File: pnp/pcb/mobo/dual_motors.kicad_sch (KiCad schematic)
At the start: 9 parts, among them M5 MOTOR1, M6 MOTOR2

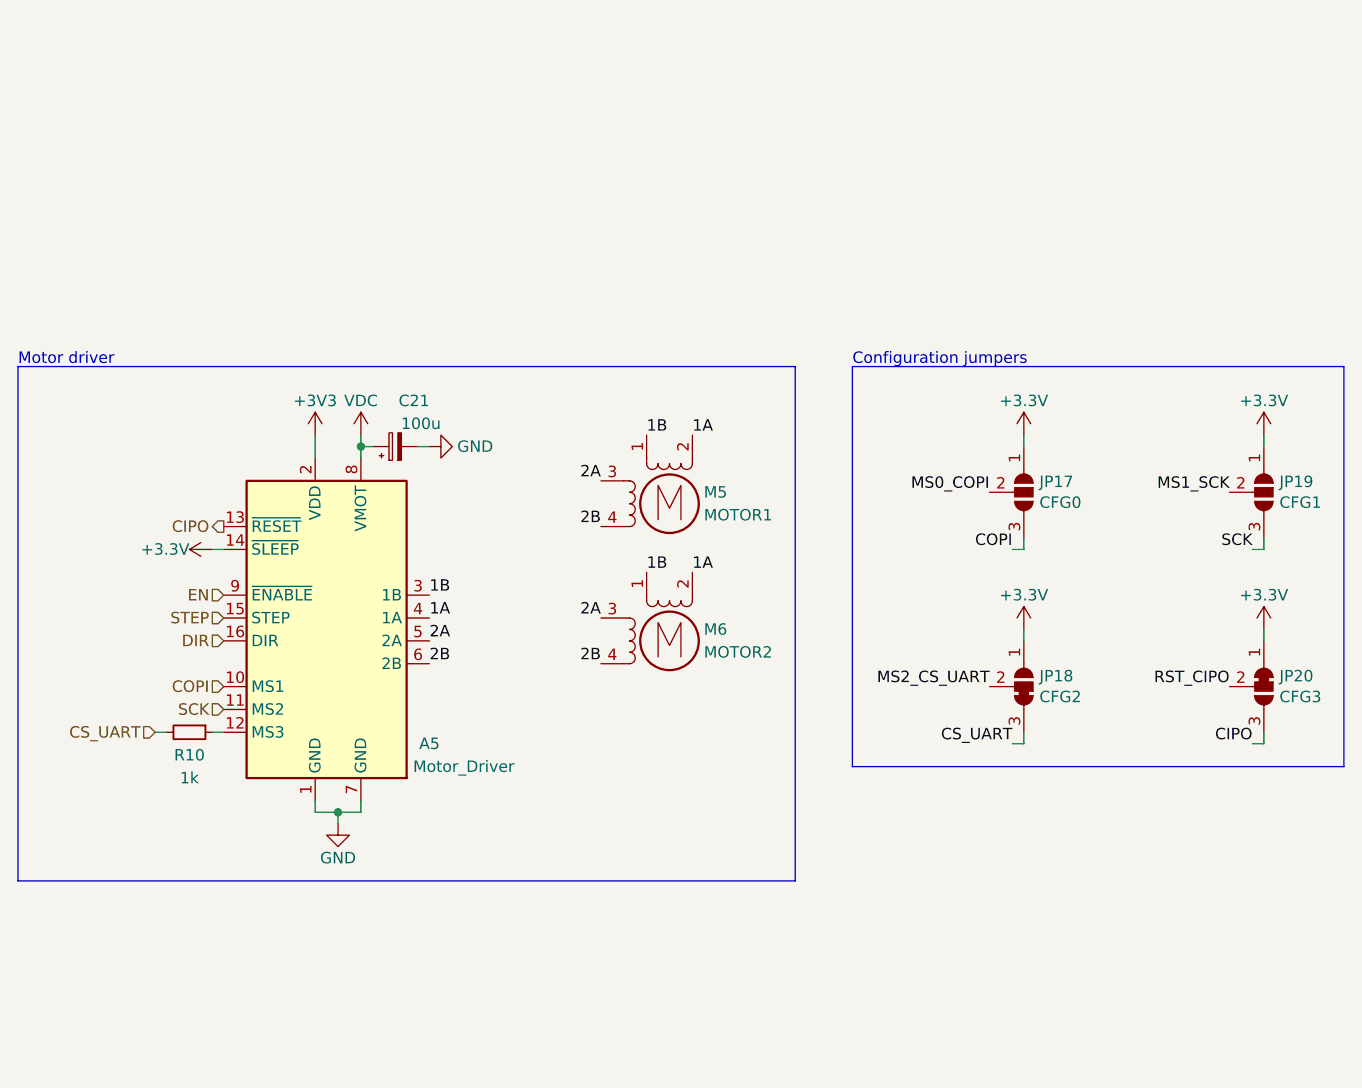
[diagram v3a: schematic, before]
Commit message: Connect all sub-sheets together
Refactored schematic is checked against existing lay-out.
Connectivity has stayed the same.
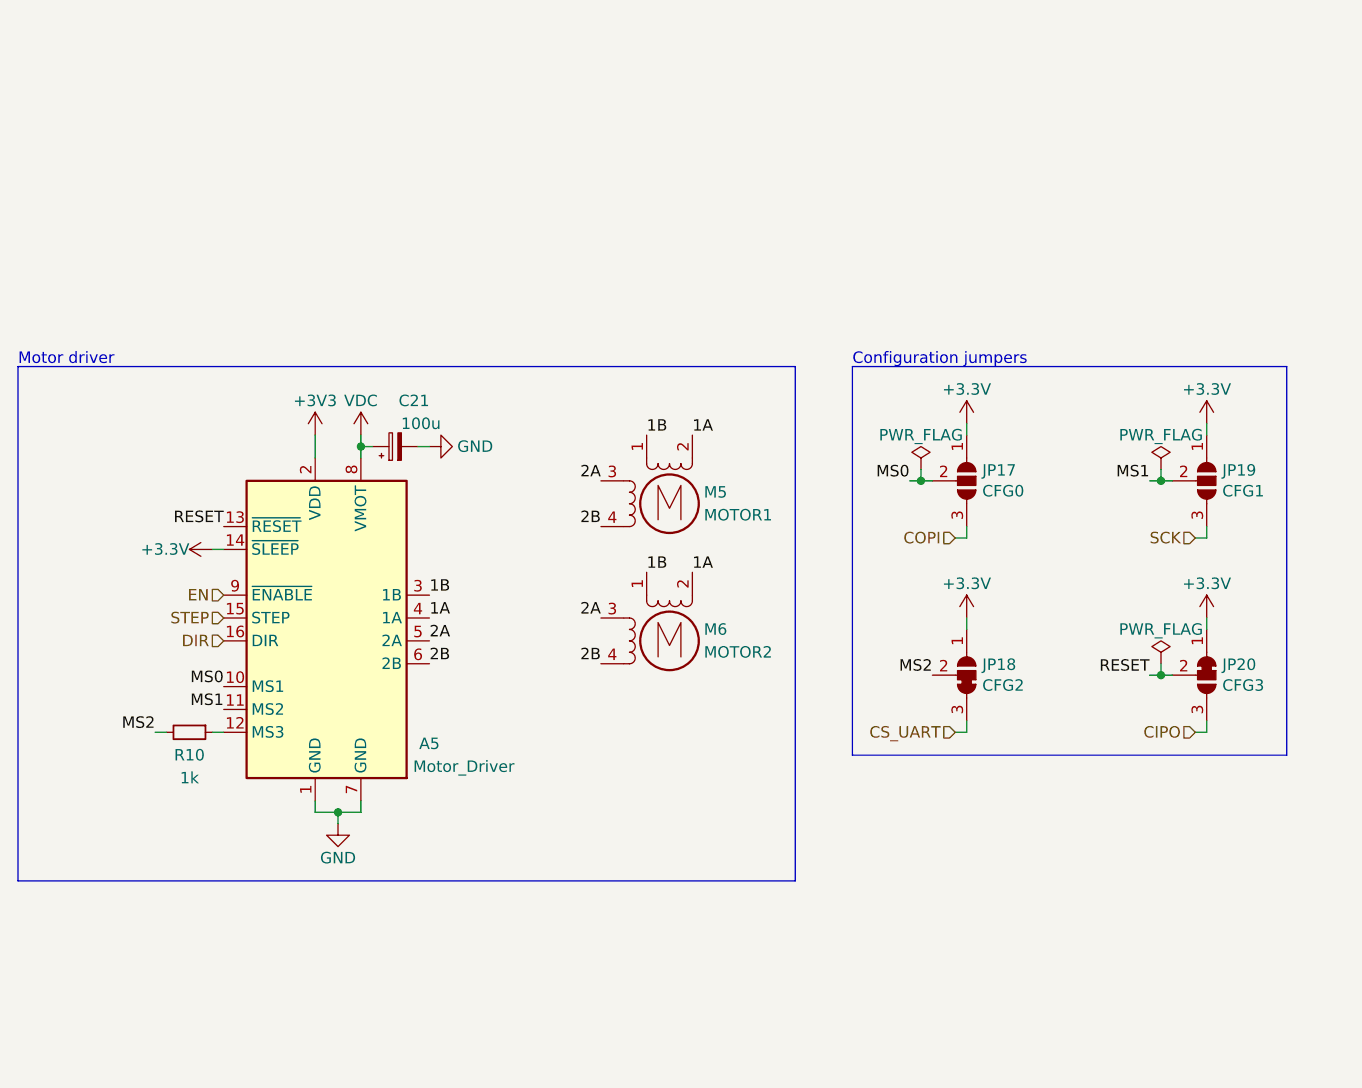
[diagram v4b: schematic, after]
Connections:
- net CIPO: no longer A5.13 (~{RESET})
- net COPI: no longer A5.10 (MS1)
- net CS_UART: no longer R10.2
- net SCK: no longer A5.11 (MS2)
- net MS0_COPI renamed MS0
- net MS0: now also A5.10 (MS1)
- net MS1_SCK renamed MS1
- net MS1: now also A5.11 (MS2)
- net MS2_CS_UART renamed MS2
- net MS2: now also R10.2
- net RST_CIPO renamed RESET
- net RESET: now also A5.13 (~{RESET})
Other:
- moved on the sheet: JP17, JP18, JP19, JP20

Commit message: Fixed schematic parity
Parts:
- JP18: footprint index:SolderJumper-3_P1.3mm_Bridged23_RoundedPad1.0x1.5mm -> (none)
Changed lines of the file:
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@@
     (effects (font (size 1.27 1.27)) (justify right))
   )
-  (symbol (lib_id "power:+3V3") (at 116.84 85.09 0)
+  (symbol (lib_id "power:+3V3") (at 116.84 85.09 0) (unit 1)
     (in_bom yes) (on_board yes)
     (property "Reference" "#PWR066" (id 0) (at 116.84 88.9 0)
@@
     (pin "1")
   )
-  (symbol (lib_id "power:GND") (at 119.38 128.27 0)
+  (symbol (lib_id "power:GND") (at 119.38 128.27 0) (unit 1)
     (in_bom yes) (on_board yes)
     (property "Reference" "#PWR067" (id 0) (at 119.38 134.62 0)
@@
     (pin "1")
   )
-  (symbol (lib_id "power:+3.3V") (at 105.41 97.79 90)
+  (symbol (lib_id "power:+3.3V") (at 105.41 97.79 90) (unit 1)
     (in_bom yes) (on_board yes)
     (property "Reference" "#PWR065" (id 0) (at 109.22 97.79 0)
@@
     (pin "1")
   )
-  (symbol (lib_id "Motor:Stepper_Motor_bipolar") (at 156.21 107.95 0)
+  (symbol (lib_id "Motor:Stepper_Motor_bipolar") (at 156.21 107.95 0) (unit 1)
     (in_bom yes) (on_board yes)
     (property "Reference" "M6" (id 0) (at 160.02 106.68 0)
@@
     (pin "4")
   )
-  (symbol (lib_id "Motor:Stepper_Motor_bipolar") (at 156.21 92.71 0)
+  (symbol (lib_id "Motor:Stepper_Motor_bipolar") (at 156.21 92.71 0) (unit 1)
     (in_bom yes) (on_board yes)
     (property "Reference" "M5" (id 0) (at 160.02 91.44 0)
@@
     (pin "4")
   )
-  (symbol (lib_id "Driver_Motor:Pololu_Breakout_A4988") (at 116.84 105.41 0)
+  (symbol (lib_id "Driver_Motor:Pololu_Breakout_A4988") (at 116.84 105.41 0) (unit 1)
     (in_bom yes) (on_board yes)
     (property "Reference" "A5" (id 0) (at 129.54 119.38 0))
@@
     (pin "9")
   )
-  (symbol (lib_id "power:VDC") (at 121.92 85.09 0)
+  (symbol (lib_id "power:VDC") (at 121.92 85.09 0) (unit 1)
     (in_bom yes) (on_board yes)
     (property "Reference" "#PWR068" (id 0) (at 121.92 87.63 0)
@@
     (pin "1")
   )
-  (symbol (lib_id "Device:C_Polarized_Small") (at 125.73 86.36 90)
+  (symbol (lib_id "Device:C_Polarized_Small") (at 125.73 86.36 90) (unit 1)
     (in_bom yes) (on_board yes)
     (property "Reference" "C21" (id 0) (at 129.54 81.28 90)
@@
     (pin "2")
   )
-  (symbol (lib_id "power:GND") (at 129.54 86.36 90)
+  (symbol (lib_id "power:GND") (at 129.54 86.36 90) (unit 1)
     (in_bom yes) (on_board yes)
     (property "Reference" "#PWR072" (id 0) (at 135.89 86.36 0)
@@
     (pin "1")
   )
-  (symbol (lib_id "power:+3.3V") (at 215.9 105.41 0)
+  (symbol (lib_id "power:+3.3V") (at 215.9 105.41 0) (unit 1)
     (in_bom yes) (on_board yes)
     (property "Reference" "#PWR070" (id 0) (at 215.9 109.22 0)
@@
     (pin "1")
   )
-  (symbol (lib_id "power:+3.3V") (at 189.23 83.82 0)
+  (symbol (lib_id "power:+3.3V") (at 189.23 83.82 0) (unit 1)
     (in_bom yes) (on_board yes)
     (property "Reference" "#PWR063" (id 0) (at 189.23 87.63 0)
@@
     (pin "1")
   )
-  (symbol (lib_id "power:+3.3V") (at 215.9 83.82 0)
+  (symbol (lib_id "power:+3.3V") (at 215.9 83.82 0) (unit 1)
     (in_bom yes) (on_board yes)
     (property "Reference" "#PWR069" (id 0) (at 215.9 87.63 0)
@@
     (pin "1")
   )
-  (symbol (lib_id "power:+3.3V") (at 189.23 105.41 0)
+  (symbol (lib_id "power:+3.3V") (at 189.23 105.41 0) (unit 1)
     (in_bom yes) (on_board yes)
     (property "Reference" "#PWR064" (id 0) (at 189.23 109.22 0)
@@
     (pin "1")
   )
-  (symbol (lib_id "Jumper:SolderJumper_3_Open") (at 189.23 90.17 270)
+  (symbol (lib_id "Jumper:SolderJumper_3_Open") (at 189.23 90.17 270) (unit 1)
     (in_bom yes) (on_board yes)
     (property "Reference" "JP17" (id 0) (at 190.9572 89.0016 90)
@@
     (pin "3")
   )
-  (symbol (lib_id "Jumper:SolderJumper_3_Bridged12") (at 215.9 111.76 270)
+  (symbol (lib_id "Jumper:SolderJumper_3_Bridged12") (at 215.9 111.76 270) (unit 1)
     (in_bom yes) (on_board yes)
     (property "Reference" "JP20" (id 0) (at 217.6272 110.5916 90)
@@
     (pin "3")
   )
-  (symbol (lib_id "Jumper:SolderJumper_3_Open") (at 215.9 90.17 270)
+  (symbol (lib_id "Jumper:SolderJumper_3_Open") (at 215.9 90.17 270) (unit 1)
     (in_bom yes) (on_board yes)
     (property "Reference" "JP19" (id 0) (at 217.6272 89.0016 90)
@@
     (pin "3")
   )
-  (symbol (lib_id "Device:R_Small") (at 102.87 118.11 270)
+  (symbol (lib_id "Device:R_Small") (at 102.87 118.11 270) (unit 1)
     (in_bom yes) (on_board yes)
     (property "Reference" "R10" (id 0) (at 102.87 120.65 90))
@@
     (pin "2")
   )
-  (symbol (lib_id "index:SolderJumper_3_Bridged23") (at 189.23 111.76 270) (mirror x)
+  (symbol (lib_id "index:SolderJumper_3_Bridged23") (at 189.23 111.76 270) (mirror x) (unit 1)
     (in_bom yes) (on_board yes)
     (property "Reference" "JP18" (id 0) (at 190.9572 110.5916 90)
@@
       (effects (font (size 1.27 1.27)) (justify left))
     )
-    (property "Footprint" "index:SolderJumper-3_P1.3mm_Bridged23_RoundedPad1.0x1.5mm" (id 2) (at 189.23 111.76 0)
+    (property "Footprint" "" (id 2) (at 189.23 111.76 0)
       (effects (font (size 1.27 1.27)) hide)
     )
@@
     (pin "3")
   )
-  (symbol (lib_id "power:PWR_FLAG") (at 210.82 88.9 0)
+  (symbol (lib_id "power:PWR_FLAG") (at 210.82 88.9 0) (unit 1)
     (in_bom yes) (on_board yes)
     (property "Reference" "#FLG06" (id 0) (at 210.82 86.995 0)
@@
     (pin "1")
   )
-  (symbol (lib_id "power:PWR_FLAG") (at 210.82 110.49 0)
+  (symbol (lib_id "power:PWR_FLAG") (at 210.82 110.49 0) (unit 1)
     (in_bom yes) (on_board yes)
     (property "Reference" "#FLG07" (id 0) (at 210.82 108.585 0)
@@
     (pin "1")
   )
-  (symbol (lib_id "power:PWR_FLAG") (at 184.15 88.9 0)
+  (symbol (lib_id "power:PWR_FLAG") (at 184.15 88.9 0) (unit 1)
     (in_bom yes) (on_board yes)
     (property "Reference" "#FLG05" (id 0) (at 184.15 86.995 0)

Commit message: Fix symbol library
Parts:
- JP18: footprint (none) -> index:SolderJumper-3_P1.3mm_Bridged23_RoundedPad1.0x1.5mm
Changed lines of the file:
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@@
       (effects (font (size 1.27 1.27)) (justify left))
     )
-    (property "Footprint" "" (id 2) (at 189.23 111.76 0)
+    (property "Footprint" "index:SolderJumper-3_P1.3mm_Bridged23_RoundedPad1.0x1.5mm" (id 2) (at 189.23 111.76 0)
       (effects (font (size 1.27 1.27)) hide)
     )

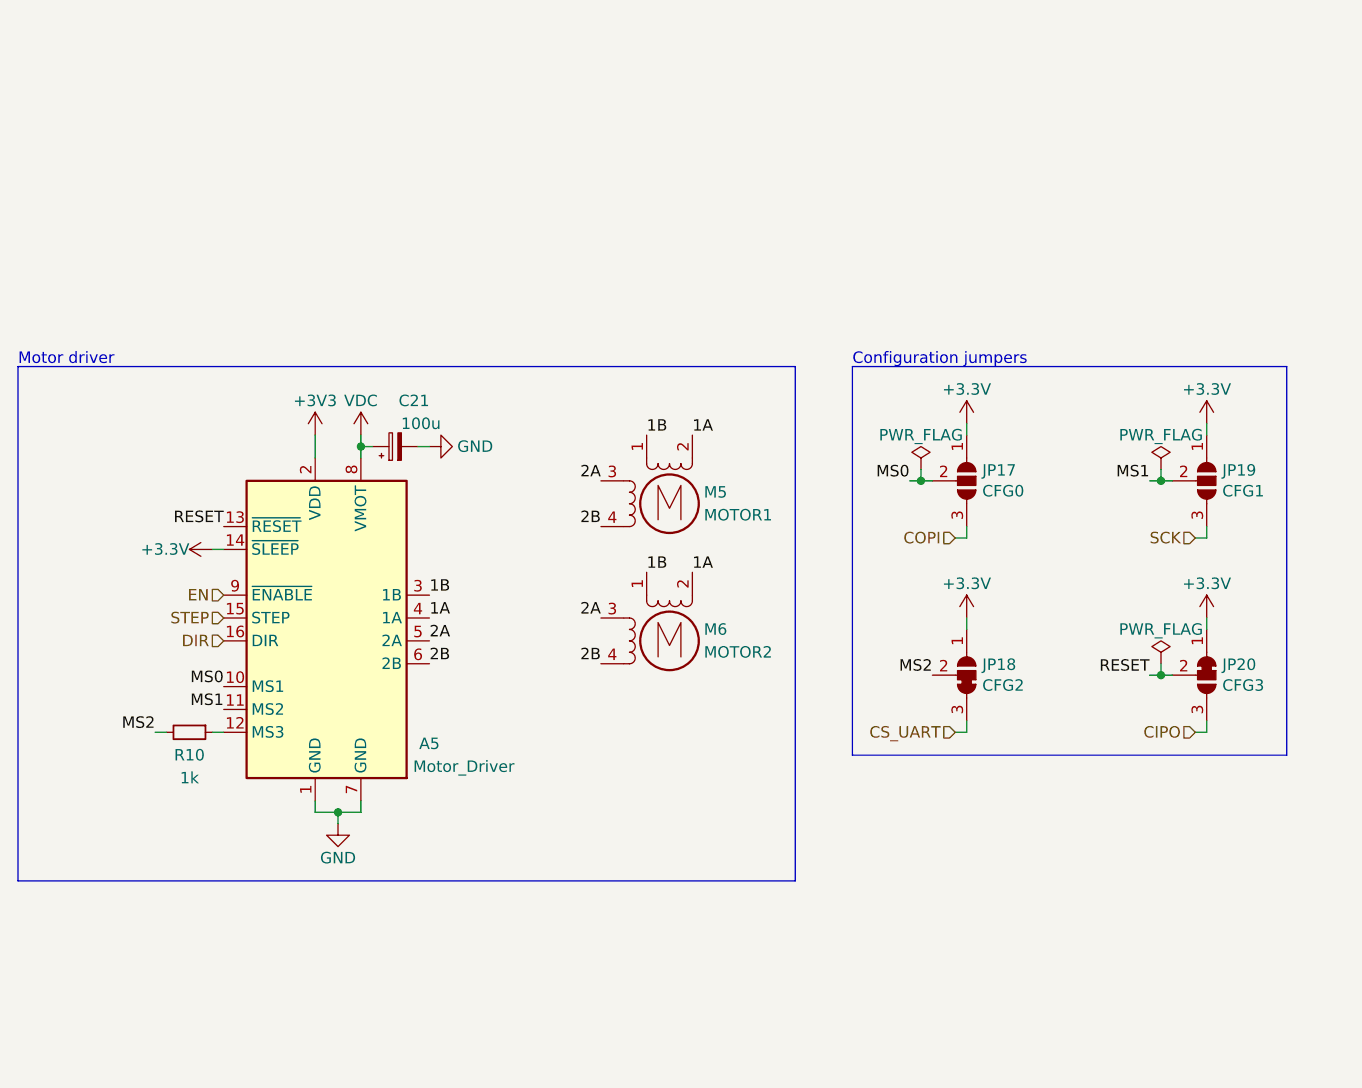
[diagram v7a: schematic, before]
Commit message: moving mobo-rev04b0 into mobo-rev04 branch from old repo
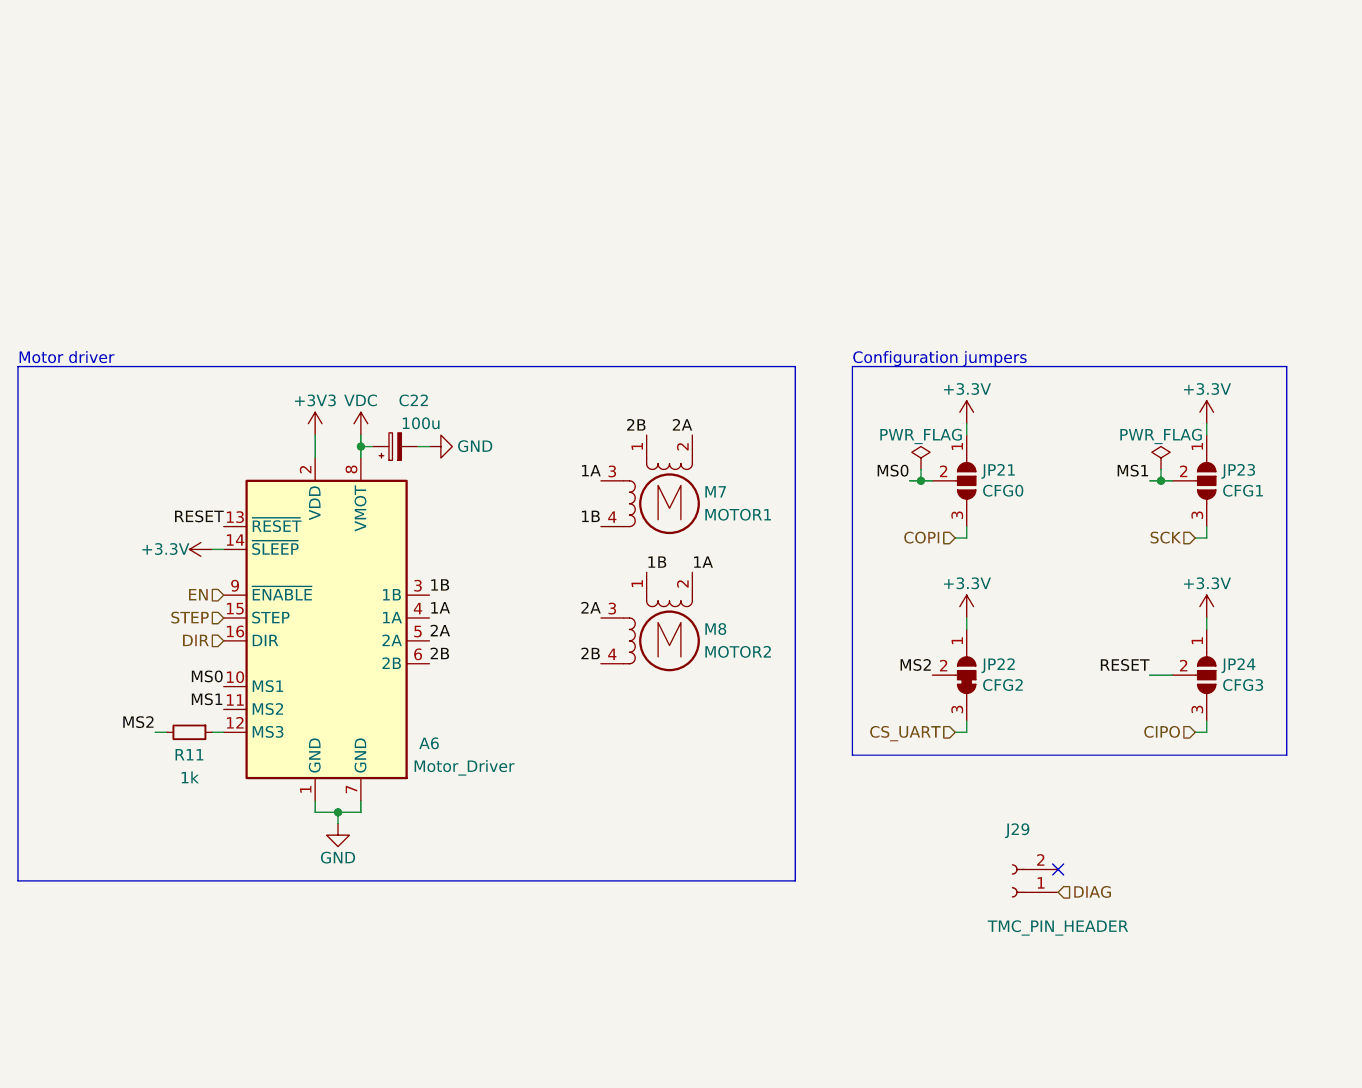
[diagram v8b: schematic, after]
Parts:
- removed JP20: CFG3, Jumper:SolderJumper-3_P1.3mm_Bridged12_RoundedPad1.0x1.5mm, symbol Jumper:SolderJumper_3_Bridged12
- added J29: TMC_PIN_HEADER, Connector_PinSocket_2.54mm:PinSocket_1x02_P2.54mm_Vertical, symbol Connector:Conn_01x02_Female
- added JP24: CFG3, Jumper:SolderJumper-3_P1.3mm_Open_RoundedPad1.0x1.5mm, symbol Jumper:SolderJumper_3_Open
- renumbered A5 to A6, C21 to C22, JP17 to JP21, JP18 to JP22, JP19 to JP23, M5 to M7, M6 to M8, R10 to R11
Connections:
- net +3V3: now also JP24.1 (A)
- net 1A: now also M7.3; no longer M7.2 (-)
- net 1B: now also M7.4; no longer M7.1
- net 2A: now also M7.2 (-); no longer M7.3
- net 2B: now also M7.1; no longer M7.4
- net CIPO: now also JP24.3 (B)
- net RESET: now also JP24.2 (C)
- new net DIAG: J29.1 (Pin_1)
- no-connect marks 0 -> 1
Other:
- company: (none) -> Opulo
- title: (none) -> LumenPnP Motherboard
